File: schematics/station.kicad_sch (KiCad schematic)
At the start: 16 parts, among them J1 USB_C_Receptacle, J2 Conn_01x04_Pin, J3 Conn_02x05_Odd_Even, SW1 SW_Push, U1 ESP32-C3-MINI-1, U2 AP2112K-3.3

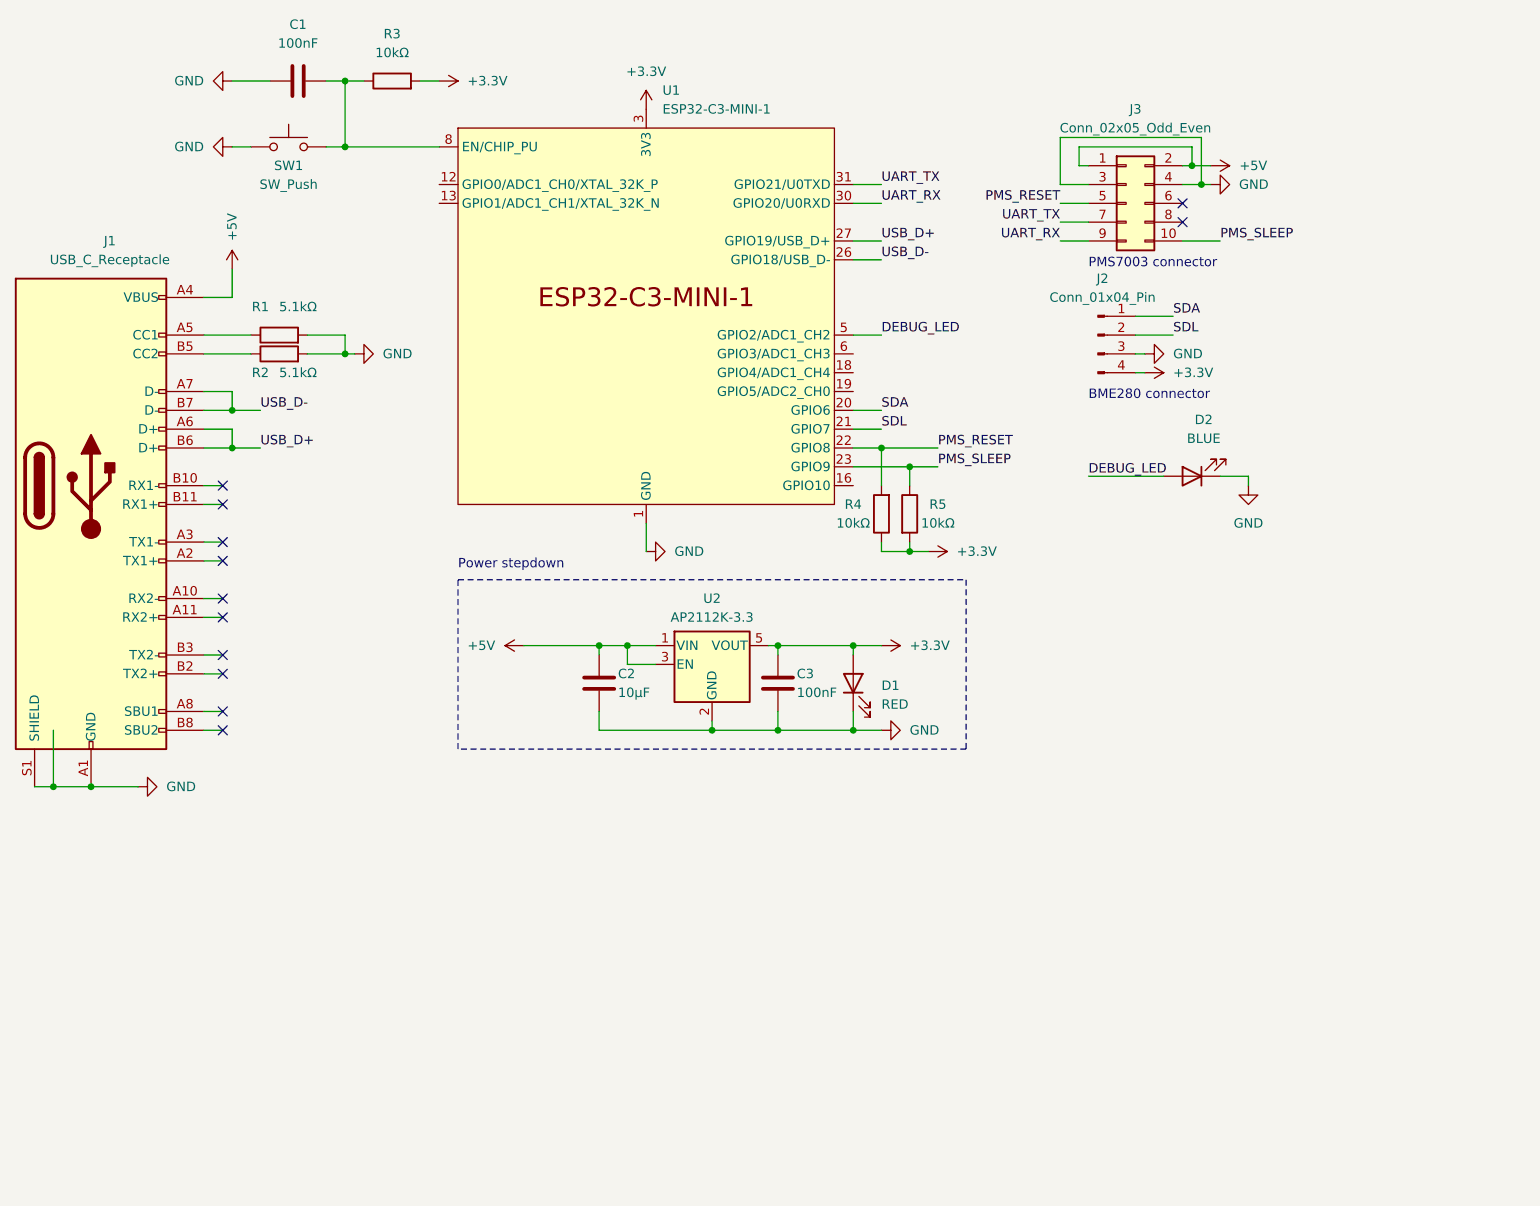
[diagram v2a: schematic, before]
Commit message: Added the ICs responsible for handling the battery
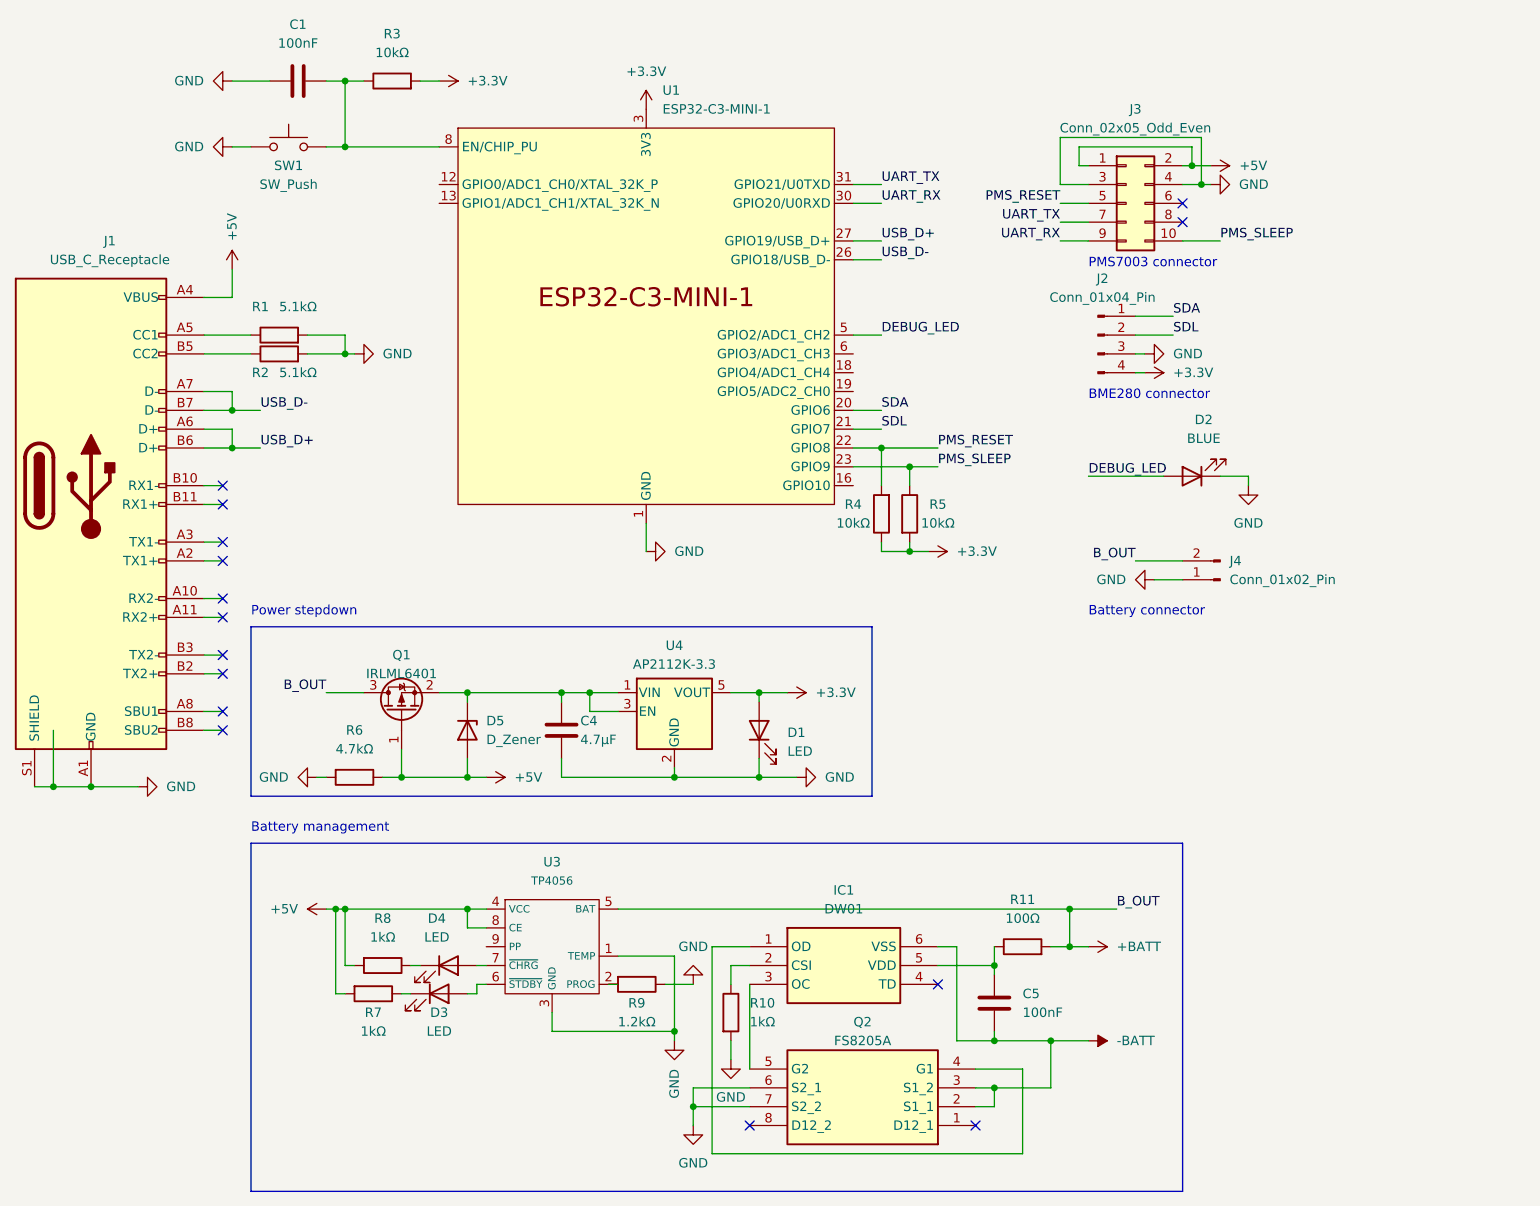
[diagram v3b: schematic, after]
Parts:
- removed C2: 10µF, Capacitor_SMD:C_0805_2012Metric_Pad1.18x1.45mm_HandSolder, symbol Device:C
- removed C3: 100nF, Capacitor_SMD:C_0805_2012Metric_Pad1.18x1.45mm_HandSolder, symbol Device:C
- removed U2: AP2112K-3.3, Package_TO_SOT_SMD:SOT-23-5, symbol Regulator_Linear:AP2112K-3.3
- added C4: 4.7µF, Capacitor_SMD:C_0805_2012Metric_Pad1.18x1.45mm_HandSolder, symbol Device:C
- added C5: 100nF, Capacitor_SMD:C_0805_2012Metric_Pad1.18x1.45mm_HandSolder, symbol Device:C
- added D3, D4: LED, LED_SMD:LED_1812_4532Metric_Pad1.30x3.40mm_HandSolder, symbol Device:LED
- added D5: D_Zener, Diode_SMD:D_SMA_Handsoldering, symbol Device:D_Zener
- added IC1: DW01, SOT95P280X135-6N, symbol DW01A-G:DW01
- added J4: Conn_01x02_Pin, Connector_JST:JST_ACH_BM02B-ACHSS-GAN-ETF_1x02-1MP_P1.20mm_Vertical, symbol Connector:Conn_01x02_Pin
- added Q1: IRLML6401, Package_TO_SOT_SMD:SOT-23, symbol Transistor_FET:IRLML6401
- added Q2: FS8205A, FS805A:SOP65P640X120-8N, symbol FS8205A:FS8205A
- added R10, R7, R8: 1kΩ, Resistor_SMD:R_1206_3216Metric, symbol Device:R
- added R11: 100Ω, Resistor_SMD:R_1206_3216Metric, symbol Device:R
- added R6: 4.7kΩ, Resistor_SMD:R_1206_3216Metric, symbol Device:R
- added R9: 1.2kΩ, Resistor_SMD:R_1206_3216Metric, symbol Device:R
- added U3: TP4056, Package_SO:SOIC-8-1EP_3.9x4.9mm_P1.27mm_EP2.29x3mm, symbol tp4056:TP4056
- added U4: AP2112K-3.3, Package_TO_SOT_SMD:SOT-23-5, symbol Regulator_Linear:AP2112K-3.3
- D1: value RED -> LED; footprint LED_SMD:LED_0805_2012Metric_Pad1.15x1.40mm_HandSolder -> LED_SMD:LED_1812_4532Metric_Pad1.30x3.40mm_HandSolder
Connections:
- net +3.3V: now also U4.5 (VOUT)
- net +5V: now also D5.2 (A), Q1.1 (G), R6.1, R7.2, R8.2, U3.4 (VCC), U3.8 (CE)
- net GND: now also C4.2, J4.1 (Pin_1), Q2.6 (S2_1), Q2.7 (S2_2), R10.2, R6.2, R9.1, U3.1 (TEMP), U3.3 (GND), U4.2 (GND)
- new net: R9.2, U3.2 (PROG)
- new net: D3.2 (A), U3.6 (~{STDBY})
- new net: D4.2 (A), U3.7 (~{CHRG})
- new net: D4.1 (K), R8.1
- new net: C5.1, IC1.5 (VDD), R11.1
- new net: C4.1, D5.1 (K), Q1.2 (S), U4.1 (VIN), U4.3 (EN)
- new net: IC1.2 (CSI), R10.1
- new net: IC1.1 (OD), Q2.4 (G1)
- new net: IC1.3 (OC), Q2.5 (G2)
- new net: D3.1 (K), R7.1
- new net +BATT: J4.2 (Pin_2), Q1.3 (D), R11.2, U3.5 (BAT)
- new net -BATT: C5.2, IC1.6 (VSS), Q2.2 (S1_1), Q2.3 (S1_2)
- no-connect marks 12 -> 15
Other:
- note added: "Battery connector"
- note added: "Battery management"

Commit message: Tweaked the power source switching circuit
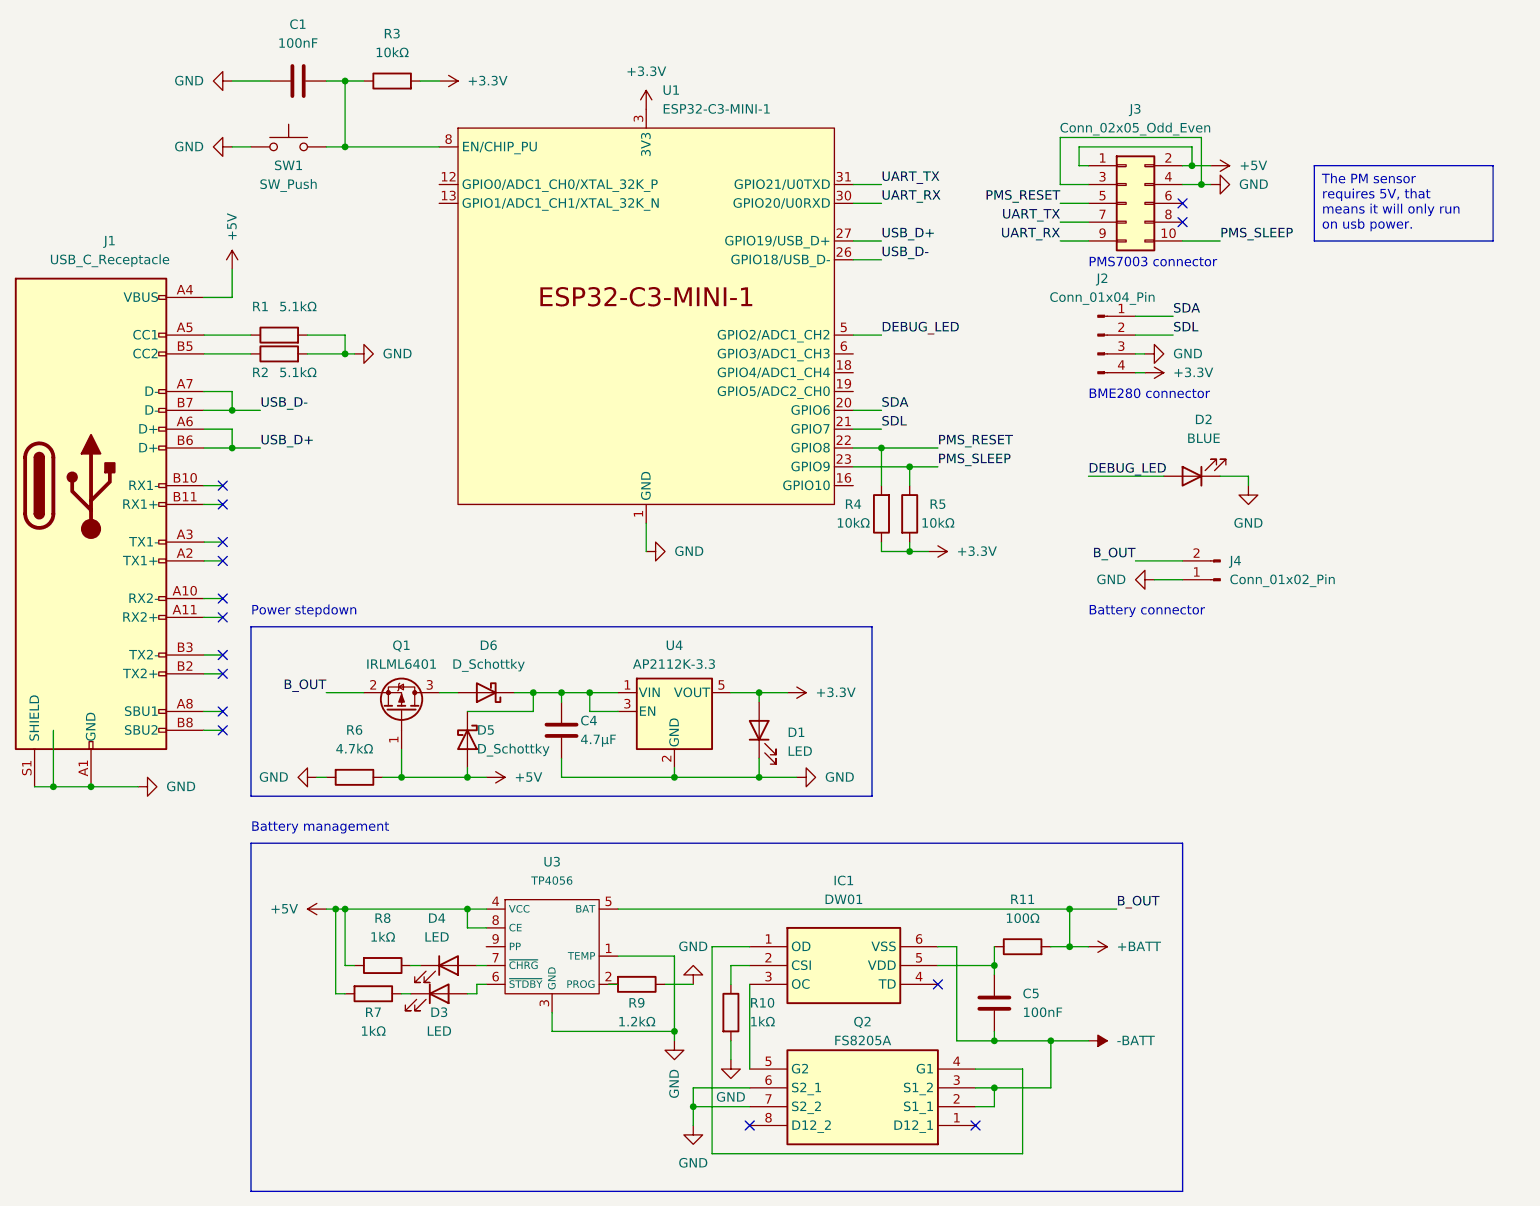
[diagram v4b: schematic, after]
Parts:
- removed D5: D_Zener, Diode_SMD:D_SMA_Handsoldering, symbol Device:D_Zener
- added D5, D6: D_Schottky, Diode_SMD:D_SOD-323_HandSoldering, symbol Device:D_Schottky
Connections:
- net +5V: now also D5.2 (A)
- net +BATT: now also Q1.2 (S); no longer Q1.3 (D)
- net at C4.1, U4.1 (VIN), U4.3 (EN): now also D5.1 (K), D6.1 (K); no longer Q1.2 (S)
- new net: D6.2 (A), Q1.3 (D)
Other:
- company: (none) -> pkozak.org
- moved on the sheet: Q1
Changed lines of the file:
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@@
     (title "Weather station")
     (date "2023-09-02")
-    (comment 1 "pkozak.org")
+    (rev "1.1")
+    (company "pkozak.org")
   )
   (junction (at 158.75 152.4) (diameter 0) (color 0 0 0 0)
@@
   (junction (at 137.16 104.14) (diameter 0) (color 0 0 0 0)
   )
+  (junction (at 86.36 123.19) (diameter 0) (color 0 0 0 0)
+  )
   (junction (at 26.67 135.89) (diameter 0) (color 0 0 0 0)
   )
   (junction (at 176.53 54.61) (diameter 0) (color 0 0 0 0)
-  )
-  (junction (at 77.47 123.19) (diameter 0) (color 0 0 0 0)
   )
   (junction (at 133.35 90.17) (diameter 0) (color 0 0 0 0)
@@
     (stroke (width 0) (type default))
   )
+  (wire (pts (xy 73.66 123.19) (xy 76.2 123.19))
+    (stroke (width 0) (type default))
+  )
   (wire (pts (xy 148.59 176.53) (xy 156.21 176.53))
     (stroke (width 0) (type default))
@@
     (stroke (width 0) (type default))
   )
-  (wire (pts (xy 77.47 124.46) (xy 77.47 123.19))
+  (wire (pts (xy 86.36 125.73) (xy 86.36 123.19))
     (stroke (width 0) (type default))
   )
@@
     (stroke (width 0) (type default))
   )
-  (wire (pts (xy 77.47 123.19) (xy 73.66 123.19))
-    (stroke (width 0) (type default))
-  )
   (wire (pts (xy 173.99 54.61) (xy 176.53 54.61))
     (stroke (width 0) (type default))
   )
-  (wire (pts (xy 77.47 132.08) (xy 77.47 134.62))
+  (wire (pts (xy 83.82 123.19) (xy 86.36 123.19))
+    (stroke (width 0) (type default))
+  )
+  (wire (pts (xy 77.47 133.35) (xy 77.47 134.62))
     (stroke (width 0) (type default))
   )
@@
     (stroke (width 0) (type default))
   )
-  (wire (pts (xy 77.47 123.19) (xy 90.17 123.19))
+  (wire (pts (xy 86.36 123.19) (xy 90.17 123.19))
     (stroke (width 0) (type default))
   )
@@
     (stroke (width 0) (type default))
   )
+  (wire (pts (xy 86.36 125.73) (xy 77.47 125.73))
+    (stroke (width 0) (type default))
+  )
   (wire (pts (xy 101.6 100.33) (xy 101.6 104.14))
     (stroke (width 0) (type default))
@@
     (stroke (width 0) (type default))
     (fill (type none))
+  )
+  (text_box "The PM sensor requires 5V, that means it will only run on usb power."
+    (at 191.77 52.07 0) (size 24.13 10.16)
+    (stroke (width 0) (type default))
+    (fill (type none))
+    (effects (font (size 1.27 1.27)) (justify left top))
   )
   (text "BME280 connector" (at 161.29 83.82 0)
@@
     )
   )
+  (symbol (lib_id "Device:D_Schottky") (at 80.01 123.19 180) (unit 1)
+    (in_bom yes) (on_board yes) (dnp no) (fields_autoplaced)
+    (property "Reference" "D6" (at 80.3275 116.84 0)
+      (effects (font (size 1.27 1.27)))
+    )
+    (property "Value" "D_Schottky" (at 80.3275 119.38 0)
+      (effects (font (size 1.27 1.27)))
+    )
+    (property "Footprint" "Diode_SMD:D_SOD-323_HandSoldering" (at 80.01 123.19 0)
+      (effects (font (size 1.27 1.27)) hide)
+    )
+    (property "Datasheet" "~" (at 80.01 123.19 0)
+      (effects (font (size 1.27 1.27)) hide)
+    )
+    (pin "1")
+    (pin "2")
+    (instances
+      (project "station"
+        (path "/85aeb712-90fa-4269-bdea-e9fbee3a2d37"
+          (reference "D6") (unit 1)
+        )
+      )
+    )
+  )
   (symbol (lib_id "power:+3.3V") (at 73.66 40.64 270) (unit 1)
     (in_bom yes) (on_board yes) (dnp no) (fields_autoplaced)
@@
         (path "/85aeb712-90fa-4269-bdea-e9fbee3a2d37"
           (reference "#PWR08") (unit 1)
+        )
+      )
+    )
+  )
+  (symbol (lib_id "Device:D_Schottky") (at 77.47 129.54 270) (unit 1)
+    (in_bom yes) (on_board yes) (dnp no)
+    (property "Reference" "D5" (at 78.74 128.27 90)
+      (effects (font (size 1.27 1.27)) (justify left))
+    )
+    (property "Value" "D_Schottky" (at 78.74 130.81 90)
+      (effects (font (size 1.27 1.27)) (justify left))
+    )
+    (property "Footprint" "Diode_SMD:D_SOD-323_HandSoldering" (at 77.47 129.54 0)
+      (effects (font (size 1.27 1.27)) hide)
+    )
+    (property "Datasheet" "~" (at 77.47 129.54 0)
+      (effects (font (size 1.27 1.27)) hide)
+    )
+    (pin "1")
+    (pin "2")
+    (instances
+      (project "station"
+        (path "/85aeb712-90fa-4269-bdea-e9fbee3a2d37"
+          (reference "D5") (unit 1)
         )
       )
@@
     )
   )
-  (symbol (lib_id "Device:D_Zener") (at 77.47 128.27 270) (unit 1)
-    (in_bom yes) (on_board yes) (dnp no) (fields_autoplaced)
-    (property "Reference" "D5" (at 80.01 127 90)
-      (effects (font (size 1.27 1.27)) (justify left))
-    )
-    (property "Value" "D_Zener" (at 80.01 129.54 90)
-      (effects (font (size 1.27 1.27)) (justify left))
-    )
-    (property "Footprint" "Diode_SMD:D_SMA_Handsoldering" (at 77.47 128.27 0)
-      (effects (font (size 1.27 1.27)) hide)
-    )
-    (property "Datasheet" "~" (at 77.47 128.27 0)
-      (effects (font (size 1.27 1.27)) hide)
-    )
-    (pin "1")
-    (pin "2")
-    (instances
-      (project "station"
-        (path "/85aeb712-90fa-4269-bdea-e9fbee3a2d37"
-          (reference "D5") (unit 1)
-        )
-      )
-    )
-  )
   (symbol (lib_id "Device:R") (at 67.31 40.64 90) (unit 1)
     (in_bom yes) (on_board yes) (dnp no) (fields_autoplaced)
@@
   )
   (symbol (lib_id "DW01A-G:DW01") (at 115.57 157.48 0) (unit 1)
-    (in_bom yes) (on_board yes) (dnp no) (fields_autoplaced)
-    (property "Reference" "IC1" (at 128.27 149.86 0)
-      (effects (font (size 1.27 1.27)))
-    )
-    (property "Value" "DW01" (at 128.27 152.4 0)
+    (in_bom yes) (on_board yes) (dnp no)
+    (property "Reference" "IC1" (at 128.27 148.59 0)
+      (effects (font (size 1.27 1.27)))
+    )
+    (property "Value" "DW01" (at 128.27 151.13 0)
       (effects (font (size 1.27 1.27)))
     )
@@
     )
   )
-  (symbol (lib_id "Transistor_FET:IRLML6401") (at 68.58 125.73 90) (unit 1)
+  (symbol (lib_id "Transistor_FET:IRLML6401") (at 68.58 125.73 270) (mirror x) (unit 1)
     (in_bom yes) (on_board yes) (dnp no)
-    (property "Reference" "Q1" (at 68.58 118.11 90)
-      (effects (font (size 1.27 1.27)))
-    )
-    (property "Value" "IRLML6401" (at 68.58 120.65 90)
-      (effects (font (size 1.27 1.27)))
-    )
-    (property "Footprint" "Package_TO_SOT_SMD:SOT-23" (at 70.485 120.65 0)
+    (property "Reference" "Q1" (at 68.58 116.84 90)
+      (effects (font (size 1.27 1.27)))
+    )
+    (property "Value" "IRLML6401" (at 68.58 119.38 90)
+      (effects (font (size 1.27 1.27)))
+    )
+    (property "Footprint" "Package_TO_SOT_SMD:SOT-23" (at 66.675 120.65 0)
       (effects (font (size 1.27 1.27) italic) (justify left) hide)
     )
